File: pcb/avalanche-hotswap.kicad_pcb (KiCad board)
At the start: 2 copper layers, 179.7 x 122.7 mm, 138 parts, among them J1 TRRS, J2 OLED, P1 i2c_pin, P2 i2c_pin, P3 battery+, P4 battery-, SW0 SW_Push, SW1 SW_Push, SW10 SW_Push, SW11 SW_Push, SW12 SW_Push, SW13 SW_Push, SW14 SW_Push, SW15 SW_Push, SW16 SW_Push, SW17 SW_Push, SW18 SW_Push, SW19 SW_Push, SW2 SW_Push, SW20 SW_Push, SW21 SW_Push, SW22 SW_Push, SW23 SW_Push, SW24 SW_Push, SW25 SW_Push, SW26 SW_Push, SW27 SW_Push, SW28 SW_Push, SW29 SW_Push, SW3 SW_Push, SW30 SW_Push, SW31 SW_Push, SW32 SW_Push, SW33 SW_DPDT_x2, SW34 SW_DPDT_x2, SW4 SW_Push, SW5 SW_Push, SW6 SW_Push, SW7 SW_Push, SW8 SW_Push, SW9 SW_Push, U1 ProMicro

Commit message: Avalanche with palm key.
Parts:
- removed L38: SK6812MINI_LED, used_footprints:YS-SK6812MINI-E
- moved D27 41.0 mm to (83.4, 124.3)
- moved SW27 41.0 mm to (91.3, 120.3)
- moved HM5 26.4 mm to (96.8, 109.8)
- moved D28 0.47 mm to (145.9, 115.3)
- moved SW16 0.47 mm to (147.7, 73.5)
- moved SW30 0.47 mm to (177.3, 116.7)
- moved SW33 0.47 mm to (207.4, 51.6)
- moved D7 0.47 mm to (80.4, 66.2)
- moved L35 0.47 mm to (88.5, 66.8)
- moved JP1 0.47 mm to (206.2, 84.2)
- moved L10 0.47 mm to (203.6, 111.2)
- moved SW29 0.47 mm to (156.3, 114.2)
- moved SW2 0.47 mm to (106.3, 42.1)
- moved D10 0.47 mm to (128.6, 65.8)
- moved D13 0.47 mm to (85.7, 72.9)
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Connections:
- D27 pad 2: Net-(D27-Pad2) -> (no net)
- SW27 pad 1: Net-(D27-Pad2) -> (no net)
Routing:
- net Net-(L37-Pad2): track 47.7 -> 4.68 mm, vias 4 -> 1
- net row4: track 309.6 -> 272.6 mm, vias 8 -> 6
- net GND: track 1149.7 -> 1115.2 mm, vias 77 -> 75
- net (no net): track 0.09 -> 30.5 mm, vias 0 -> 1
- net Net-(D27-Pad2): track 30.4 -> 0.00 mm, vias 1 -> 0
- net VCC: track 973.6 -> 946.7 mm, vias 63 -> 62
- net col0: track 286.7 -> 300.1 mm, vias 8 -> 10
- net Net-(L38-Pad2): track 4.60 -> 0.00 mm, vias 1 -> 0
- net row3: track 215.0 -> 217.2 mm
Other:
- board size 179.7 x 122.7 mm -> 162.7 x 122.7 mm

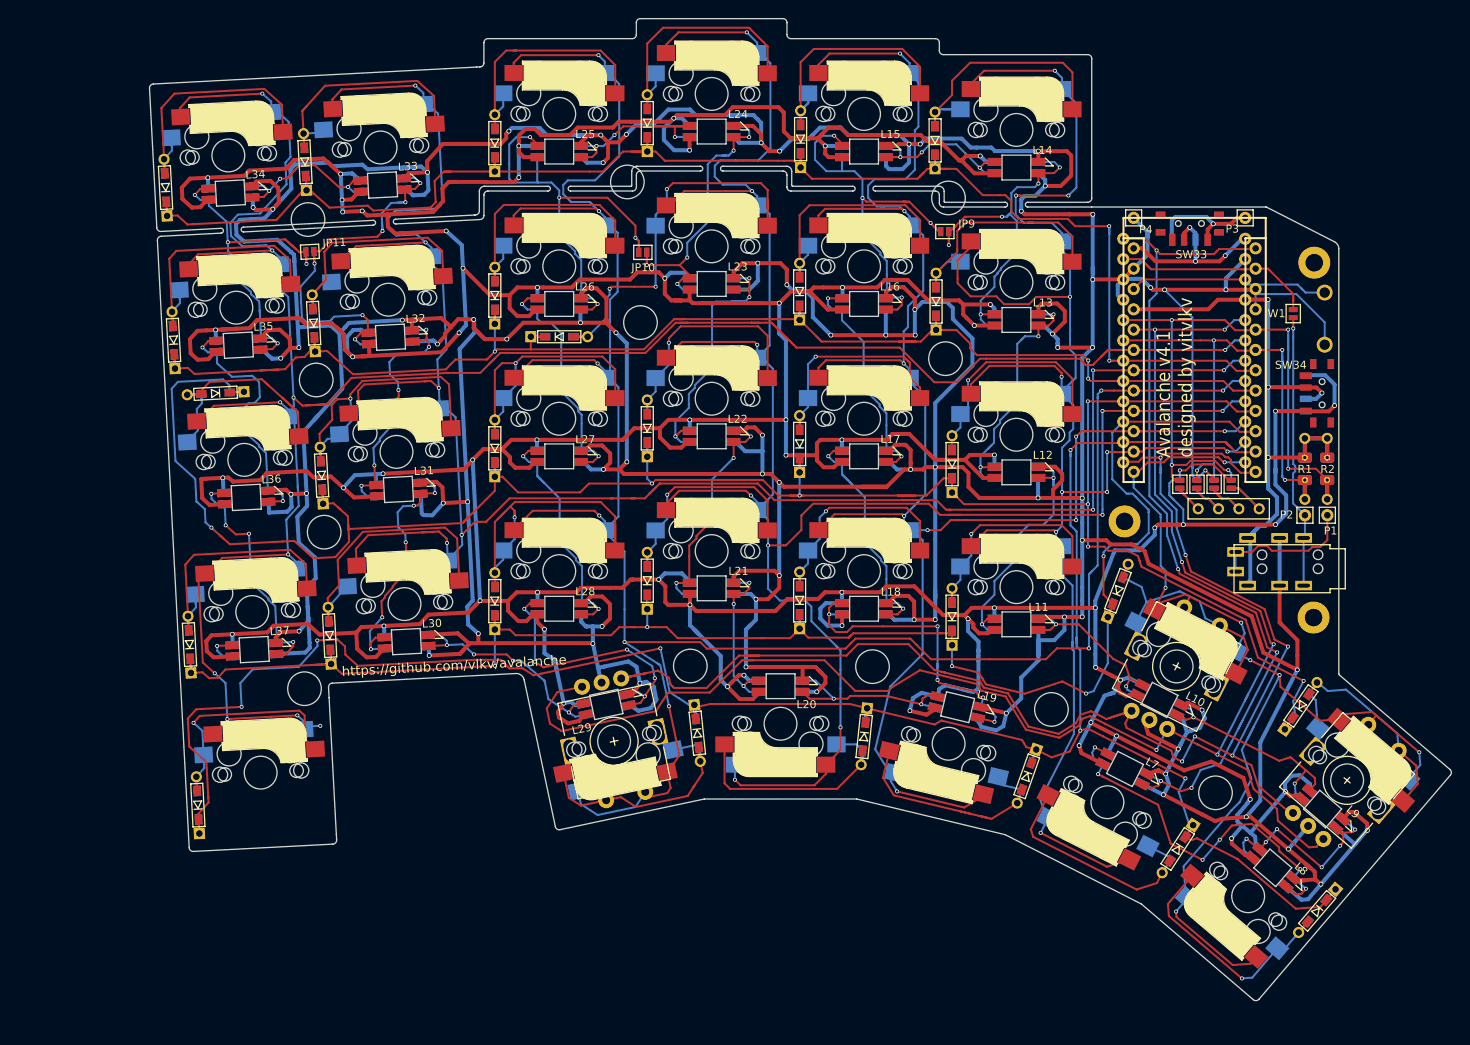
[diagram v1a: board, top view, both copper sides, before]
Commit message: Merged v4.2 into palm branch.
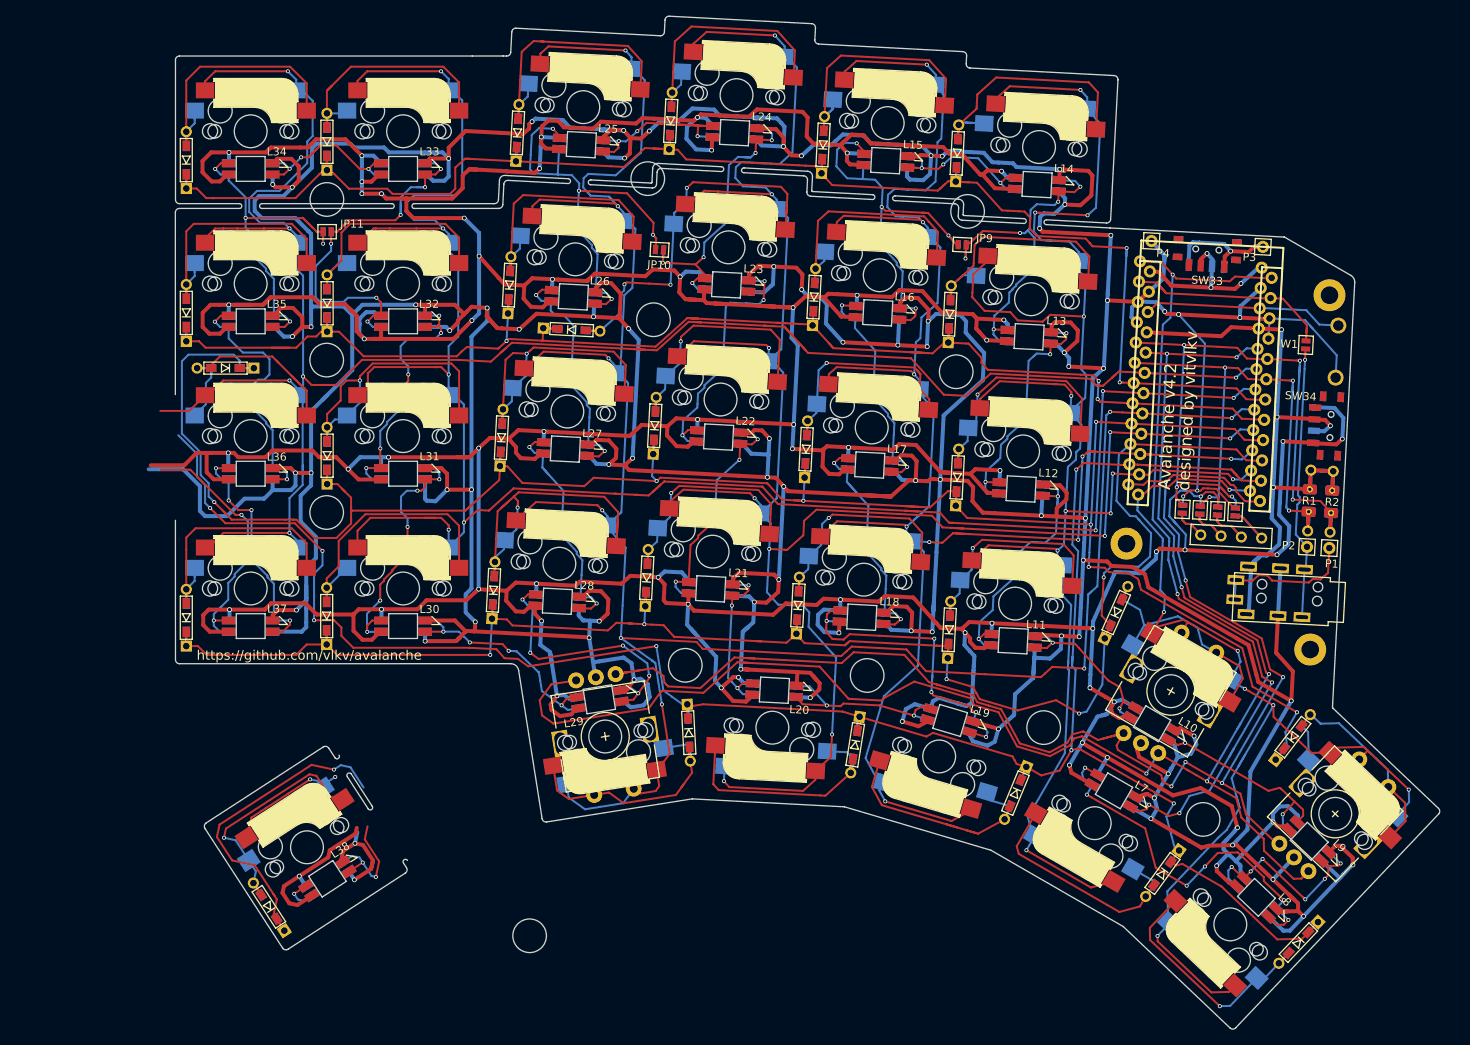
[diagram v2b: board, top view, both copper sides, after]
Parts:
- added L38: SK6812MINI_LED, used_footprints:YS-SK6812MINI-E, F.Cu at (99.6, 133.5)
- moved HM5 41.8 mm to (124.9, 140.7), turned to 0 degrees
- moved D27 15.5 mm to (92.3, 137.0), turned to 123 degrees
- moved SW27 11.0 mm to (97.1, 129.6), turned to 213 degrees
- moved D32 4.61 mm to (221.0, 141.5), turned to 226.5 degrees
- moved HM1 4.49 mm to (224.9, 60.6), turned to 337.5 degrees
- moved ENC1 4.45 mm to (225.6, 125.4), turned to 46.5 degrees
- moved SW19 4.45 mm to (225.6, 125.4), turned to 136.5 degrees
- moved SW0 4.40 mm to (225.8, 67.7), turned to 87 degrees
- moved L9 4.36 mm to (222.4, 128.8), turned to 316.5 degrees
- moved D1 4.31 mm to (82.0, 43.7), turned to 90 degrees
- moved P3 4.24 mm to (216.6, 54.6), turned to 357 degrees
- moved SW34 4.22 mm to (225.0, 76.9), turned to 87 degrees
- moved W1 4.22 mm to (221.9, 66.8), turned to 267 degrees
- moved L8 4.22 mm to (215.8, 135.9), turned to 316.5 degrees
- moved SW32 4.17 mm to (212.5, 139.2), turned to 316.5 degrees
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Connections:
- D27 pad 2: (no net) -> Net-(D27-Pad2)
- JP1 pad 2: VCC -> GND
- JP2 pad 2: GND -> VCC
- JP7 pad 2: GND -> VCC
- JP8 pad 2: VCC -> GND
- SW27 pad 1: (no net) -> Net-(D27-Pad2)
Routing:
- net Net-(L37-Pad2): track 4.68 -> 47.7 mm, vias 1 -> 4
- net GND: track 1115.2 -> 1153.8 mm, vias 75 -> 78
- net row4: track 272.6 -> 309.6 mm, vias 6 -> 8
- net Net-(D27-Pad2): track 0.00 -> 30.4 mm, vias 0 -> 1
- net (no net): track 30.5 -> 0.09 mm, vias 1 -> 0
- net VCC: track 946.7 -> 973.3 mm, vias 62 -> 63
- net col0: track 300.1 -> 286.7 mm, vias 10 -> 8
- net Net-(L38-Pad2): track 0.00 -> 4.60 mm, vias 0 -> 1
- net row3: track 217.2 -> 215.0 mm
- net SCL: track 66.0 -> 65.1 mm
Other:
- board size 162.7 x 122.7 mm -> 158 x 126.6 mm
- board text added: "Avalanche v4.2 designed by vitvlkv"
- board text removed: "Avalanche v4.1 designed by vitvlkv"

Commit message: Final changes of palm release.
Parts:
- moved HM5 34.8 mm to (99.4, 117.0)
- moved D13 13.2 mm to (81.9, 81.9), turned to 90 degrees
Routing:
- net row2: track 273.0 -> 237.5 mm, vias 7 -> 6
- net row4: track 309.6 -> 276.8 mm, vias 8 -> 4
- net col0: track 286.7 -> 318.8 mm, vias 8 -> 9
- net Net-(L37-Pad2): track 47.7 -> 54.4 mm
- net Net-(D22-Pad2): track 44.7 -> 40.1 mm
- net GND: track 1153.8 -> 1158.1 mm, vias 78 -> 77
- net Net-(L35-Pad2): track 32.4 -> 28.6 mm
- net Net-(D30-Pad2): track 32.9 -> 29.5 mm
- net Net-(D6-Pad2): track 35.8 -> 32.7 mm
- net VCC: track 973.3 -> 976.3 mm
- net row0: track 195.4 -> 192.8 mm
- net Net-(D10-Pad2): track 49.2 -> 47.1 mm
- net Net-(D2-Pad2): track 33.1 -> 32.0 mm
- net Net-(D7-Pad2): track 33.7 -> 32.6 mm
- net Net-(D1-Pad2): track 34.2 -> 33.1 mm
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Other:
- outline, holes or cut-outs redrawn
- net class Default removed
